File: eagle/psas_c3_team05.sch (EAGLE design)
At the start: 88 parts, among them IC1 CP2102, U1 MIC5319 3.3V, U2 MCP73871, X1 32 MHz

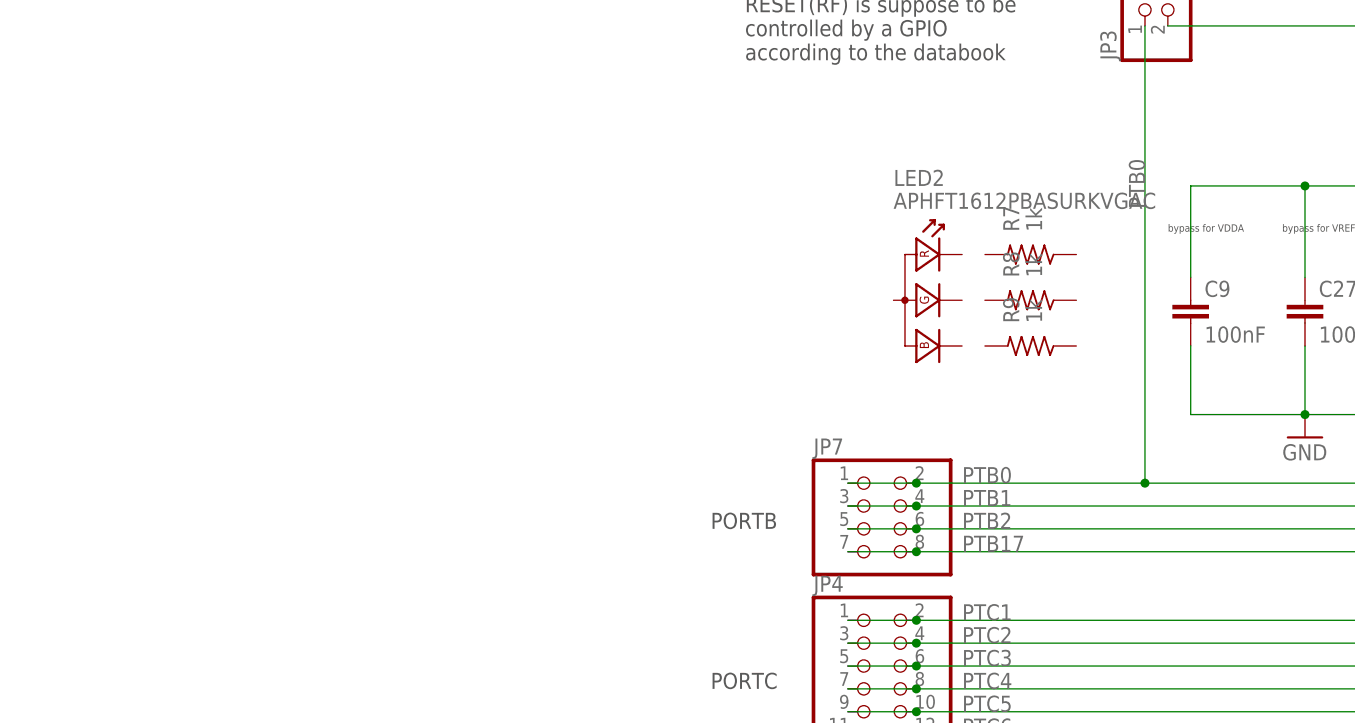
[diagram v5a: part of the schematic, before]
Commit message: added heartbeat LED to MCU on Port B
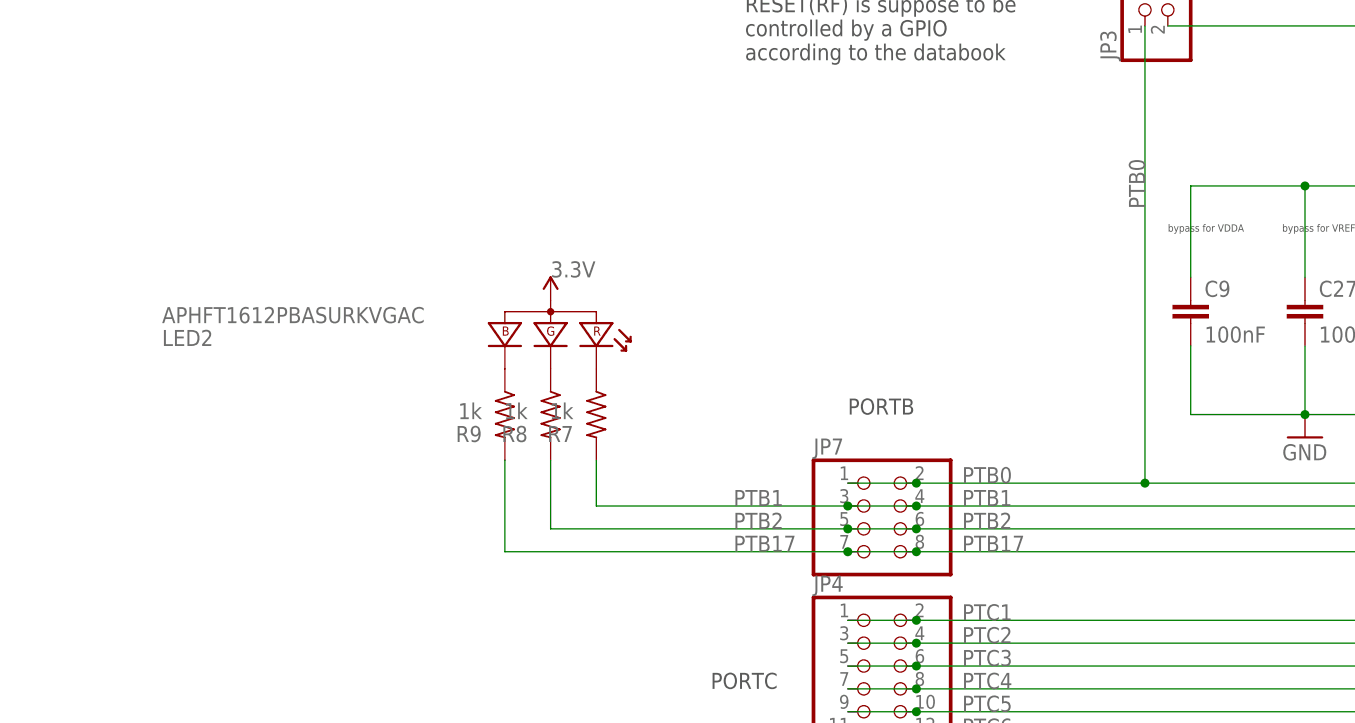
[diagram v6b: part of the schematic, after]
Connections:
- new net N$32: LED2.BK, R9.1
- new net N$33: LED2.GK, R8.1
- new net N$34: LED2.RK, R7.1
- net 3.3V: now also LED2.COMMON_ANODE
- net PTB1: now also R7.2
- net PTB17: now also R9.2
- net PTB2: now also R8.2
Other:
- moved on the sheet: LED2, R7, R8, R9
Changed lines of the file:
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@@
 <setting verticaltext="up"/>
 </settings>
-<grid distance="0.05" unitdist="inch" unit="inch" style="lines" multiple="2" display="yes" altdistance="0.01" altunitdist="inch" altunit="inch"/>
+<grid distance="0.1" unitdist="inch" unit="inch" style="lines" multiple="1" display="no" altdistance="0.01" altunitdist="inch" altunit="inch"/>
 <layers>
 <layer number="1" name="Top" color="4" fill="1" visible="no" active="no"/>
@@
 <part name="R8" library="rcl_custom" deviceset="R-US_" device="0603-B-NOSILK" value="1k"/>
 <part name="R9" library="rcl_custom" deviceset="R-US_" device="0603-B-NOSILK" value="1k"/>
+<part name="P+9" library="Vibrogait_prototype" deviceset="3.3V" device=""/>
 </parts>
 <sheets>
@@
 according to the databook</text>
 <text x="137.16" y="193.04" size="1.778" layer="97">PORTC</text>
-<text x="137.16" y="210.82" size="1.778" layer="97">PORTB</text>
+<text x="152.4" y="223.52" size="1.778" layer="97">PORTB</text>
 <text x="137.16" y="172.72" size="1.778" layer="97">PORTD</text>
 <text x="137.16" y="149.86" size="1.778" layer="97">PORTE</text>
@@
 <attribute name="VALUE" x="160.655" y="307.34" size="1.27" layer="95" rot="R270"/>
 </instance>
-<instance part="LED2" gate="LED" x="160.02" y="236.22" smashed="yes" rot="MR270">
-<attribute name="NAME" x="157.48" y="248.92" size="1.778" layer="95"/>
-<attribute name="VALUE" x="157.48" y="246.38" size="1.778" layer="96"/>
+<instance part="LED2" gate="LED" x="119.38" y="233.68" smashed="yes" rot="MR0">
+<attribute name="NAME" x="76.2" y="231.14" size="1.778" layer="95"/>
+<attribute name="VALUE" x="76.2" y="233.68" size="1.778" layer="96"/>
 </instance>
 <instance part="LED3" gate="LED" x="477.52" y="345.44" smashed="yes">
@@
 <attribute name="VALUE" x="474.98" y="325.12" size="1.778" layer="96"/>
 </instance>
-<instance part="R7" gate="R" x="172.72" y="241.3" smashed="yes" rot="R180">
-<attribute name="NAME" x="171.45" y="243.84" size="1.778" layer="95" rot="R90"/>
-<attribute name="VALUE" x="173.99" y="243.84" size="1.778" layer="96" rot="R90"/>
-</instance>
-<instance part="R8" gate="R" x="172.72" y="236.22" smashed="yes" rot="R180">
-<attribute name="NAME" x="171.45" y="238.76" size="1.778" layer="95" rot="R90"/>
-<attribute name="VALUE" x="173.99" y="238.76" size="1.778" layer="96" rot="R90"/>
-</instance>
-<instance part="R9" gate="R" x="172.72" y="231.14" smashed="yes" rot="R180">
-<attribute name="NAME" x="171.45" y="233.68" size="1.778" layer="95" rot="R90"/>
-<attribute name="VALUE" x="173.99" y="233.68" size="1.778" layer="96" rot="R90"/>
+<instance part="R7" gate="R" x="124.46" y="223.52" smashed="yes" rot="R270">
+<attribute name="NAME" x="121.92" y="222.25" size="1.778" layer="95" rot="R180"/>
+<attribute name="VALUE" x="121.92" y="224.79" size="1.778" layer="96" rot="R180"/>
+</instance>
+<instance part="R8" gate="R" x="119.38" y="223.52" smashed="yes" rot="R270">
+<attribute name="NAME" x="116.84" y="222.25" size="1.778" layer="95" rot="R180"/>
+<attribute name="VALUE" x="116.84" y="224.79" size="1.778" layer="96" rot="R180"/>
+</instance>
+<instance part="R9" gate="R" x="114.3" y="223.52" smashed="yes" rot="R270">
+<attribute name="NAME" x="111.76" y="222.25" size="1.778" layer="95" rot="R180"/>
+<attribute name="VALUE" x="111.76" y="224.79" size="1.778" layer="96" rot="R180"/>
+</instance>
+<instance part="P+9" gate="G$1" x="119.38" y="236.22" smashed="yes">
+<attribute name="VALUE" x="119.38" y="238.76" size="1.778" layer="96"/>
 </instance>
 </instances>
@@
 <junction x="309.88" y="213.36"/>
 <junction x="309.88" y="226.06"/>
+</segment>
+<segment>
+<pinref part="LED2" gate="LED" pin="COMMON_ANODE"/>
+<pinref part="P+9" gate="G$1" pin="3.3V"/>
 </segment>
 </net>
@@
 <wire x1="152.4" y1="208.28" x2="160.02" y2="208.28" width="0.1524" layer="91"/>
 <junction x="160.02" y="208.28"/>
+<pinref part="R9" gate="R" pin="2"/>
+<wire x1="152.4" y1="208.28" x2="114.3" y2="208.28" width="0.1524" layer="91"/>
+<wire x1="114.3" y1="208.28" x2="114.3" y2="218.44" width="0.1524" layer="91"/>
+<junction x="152.4" y="208.28"/>
+<label x="139.7" y="208.28" size="1.778" layer="95"/>
 </segment>
 </net>
@@
 <wire x1="152.4" y1="213.36" x2="160.02" y2="213.36" width="0.1524" layer="91"/>
 <junction x="160.02" y="213.36"/>
+<pinref part="R7" gate="R" pin="2"/>
+<wire x1="152.4" y1="213.36" x2="124.46" y2="213.36" width="0.1524" layer="91"/>
+<wire x1="124.46" y1="213.36" x2="124.46" y2="218.44" width="0.1524" layer="91"/>
+<junction x="152.4" y="213.36"/>
+<label x="139.7" y="213.36" size="1.778" layer="95"/>
 </segment>
 </net>
@@
 <wire x1="152.4" y1="210.82" x2="160.02" y2="210.82" width="0.1524" layer="91"/>
 <junction x="160.02" y="210.82"/>
+<pinref part="R8" gate="R" pin="2"/>
+<wire x1="152.4" y1="210.82" x2="119.38" y2="210.82" width="0.1524" layer="91"/>
+<wire x1="119.38" y1="210.82" x2="119.38" y2="218.44" width="0.1524" layer="91"/>
+<junction x="152.4" y="210.82"/>
+<label x="139.7" y="210.82" size="1.778" layer="95"/>
 </segment>
 </net>
@@
 </segment>
 </net>
+<net name="N$32" class="0">
+<segment>
+<pinref part="LED2" gate="LED" pin="BK"/>
+<pinref part="R9" gate="R" pin="1"/>
+</segment>
+</net>
+<net name="N$33" class="0">
+<segment>
+<pinref part="LED2" gate="LED" pin="GK"/>
+<pinref part="R8" gate="R" pin="1"/>
+</segment>
+</net>
+<net name="N$34" class="0">
+<segment>
+<pinref part="LED2" gate="LED" pin="RK"/>
+<pinref part="R7" gate="R" pin="1"/>
+</segment>
+</net>
